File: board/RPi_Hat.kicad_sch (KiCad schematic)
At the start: 39 parts, among them J1 PiHat, SW1 Pushbutton, SW2 Pushbutton, SW3 Pushbutton, SW4 Pushbutton, SW5 Pushbutton, SW6 Pushbutton, SW7 Pushbutton, SW8 Pushbutton

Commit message: pcb_completly_wired
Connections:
- net Button 1: now also J1.36 (BCM16); no longer J1.22 (BCM25)
- net Button 2: now also J1.38 (BCM20_MOSI); no longer J1.24 (BCM8_CE0)
- net Button 3: now also J1.31 (BCM6); no longer J1.26 (BCM7_CE1)
- net Button 4: now also J1.35 (BCM19_MISO); no longer J1.28 (BCM1_ID_SC)
- net Button 6: now also J1.37 (BCM26); no longer J1.36 (BCM16)
- net Button 7: now also J1.33 (BCM13); no longer J1.38 (BCM20_MOSI)
- net Diode 3: now also J1.22 (BCM25); no longer J1.27 (BCM0_ID_SD)
- net Diode 4: now also J1.24 (BCM8_CE0); no longer J1.29 (BCM5)
- net Diode 5: now also J1.26 (BCM7_CE1); no longer J1.31 (BCM6)
- net Diode 6: now also J1.27 (BCM0_ID_SD); no longer J1.33 (BCM13)
- net Diode 7: now also J1.28 (BCM1_ID_SC); no longer J1.35 (BCM19_MISO)
- net Diode 8: now also J1.29 (BCM5); no longer J1.37 (BCM26)
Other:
- title: (none) -> Rasperry Pi Shield

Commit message: transistors
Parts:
- removed C1: 100n, HWP:C_0805, symbol HWP:C
- added Q1, Q2, Q3, Q4, Q5, Q6, Q7, Q8: (no value), symbol HWP:PMOS_GSD
- J1: value PiHat -> (none); footprint HWP:PiHeader -> (none)
- R10, R9: value 10k -> 4.7k
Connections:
- net +3V3: now also Q1.3 (D), Q2.3 (D), Q3.3 (D), Q4.3 (D), Q5.3 (D), Q6.3 (D), Q7.3 (D), Q8.3 (D)
- net Button 1: now also J1.33 (BCM13); no longer J1.36 (BCM16)
- net Button 2: now also J1.31 (BCM6); no longer J1.38 (BCM20_MOSI)
- net Button 3: now also J1.32 (BCM12); no longer J1.31 (BCM6)
- net Button 4: now also J1.29 (BCM5); no longer J1.35 (BCM19_MISO)
- net Button 5: now also J1.36 (BCM16); no longer J1.32 (BCM12)
- net Button 6: now also J1.35 (BCM19_MISO); no longer J1.37 (BCM26)
- net Button 7: now also J1.37 (BCM26); no longer J1.33 (BCM13)
- net Button 8: now also J1.38 (BCM20_MOSI); no longer J1.40 (BCM21_SCLK)
- net Diode 1: now also J1.15 (BCM22), Q1.1 (G); no longer J1.21 (BCM9_MISO), R11.1
- net Diode 2: now also J1.13 (BCM27_PCM_D), Q2.1 (G); no longer J1.23 (BCM11_SCLK), R12.1
- net Diode 3: now also J1.24 (BCM8_CE0), Q3.1 (G); no longer J1.22 (BCM25), R13.1
- net Diode 4: now also J1.23 (BCM11_SCLK), Q4.1 (G); no longer J1.24 (BCM8_CE0), R14.1
- net Diode 5: now also J1.22 (BCM25), Q5.1 (G); no longer J1.26 (BCM7_CE1), R15.1
- net Diode 6: now also J1.21 (BCM9_MISO), Q6.1 (G); no longer J1.27 (BCM0_ID_SD), R16.1
- net Diode 7: now also J1.27 (BCM0_ID_SD), Q7.1 (G); no longer J1.28 (BCM1_ID_SC), R17.1
- net Diode 8: now also J1.28 (BCM1_ID_SC), Q8.1 (G); no longer J1.29 (BCM5), R18.1
- new net: Q4.2 (S), R14.1
- new net: Q6.2 (S), R16.1
- new net: Q2.2 (S), R12.1
- new net: Q1.2 (S), R11.1
- new net: Q3.2 (S), R13.1
- new net: Q5.2 (S), R15.1
- new net: Q7.2 (S), R17.1
- new net: Q8.2 (S), R18.1
- no-connect marks 13 -> 11

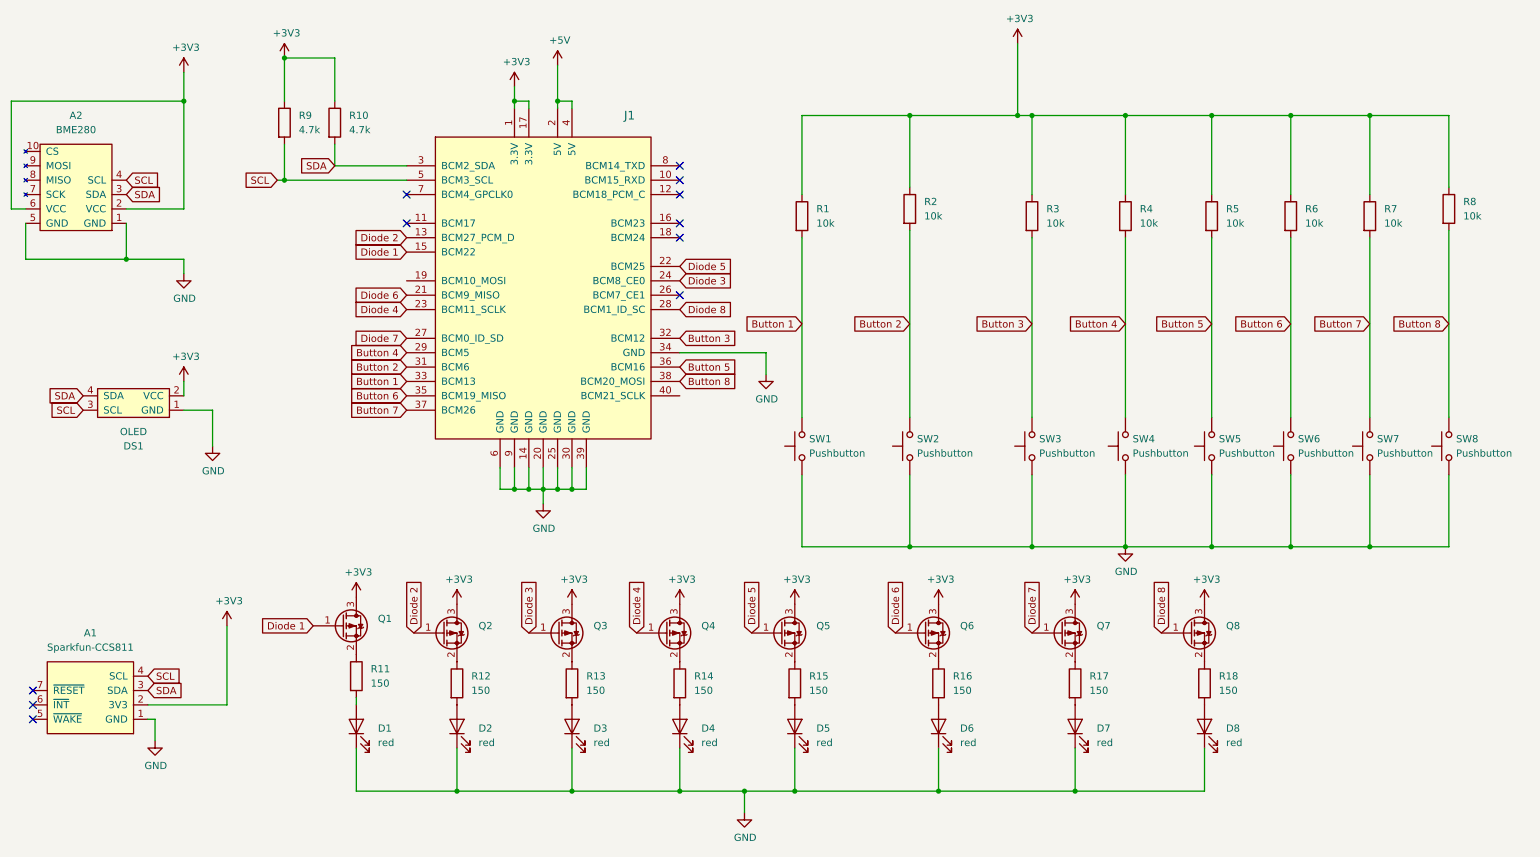
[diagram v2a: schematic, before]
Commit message: reinserted correct scematic
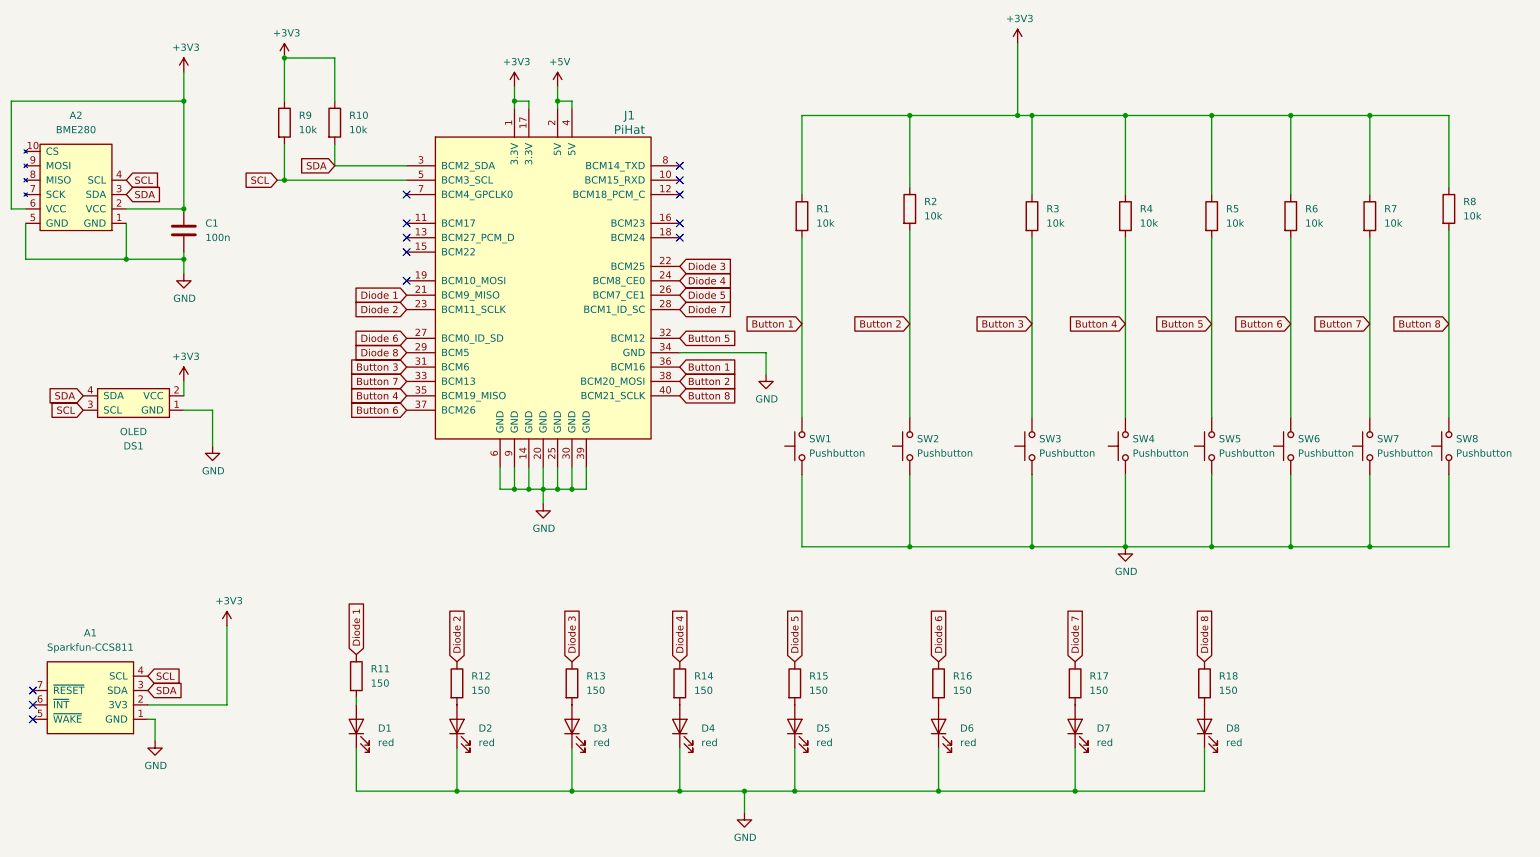
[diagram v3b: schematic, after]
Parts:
- removed Q1, Q2, Q3, Q4, Q5, Q6, Q7, Q8: (no value), symbol HWP:PMOS_GSD
- added C1: 100n, HWP:C_0805, symbol HWP:C
- J1: value (none) -> PiHat; footprint (none) -> HWP:PiHeader
- R10, R9: value 4.7k -> 10k
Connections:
- net +3V3: now also C1.1
- net Button 1: now also J1.36 (BCM16); no longer J1.33 (BCM13)
- net Button 2: now also J1.38 (BCM20_MOSI); no longer J1.31 (BCM6)
- net Button 3: now also J1.31 (BCM6); no longer J1.32 (BCM12)
- net Button 4: now also J1.35 (BCM19_MISO); no longer J1.29 (BCM5)
- net Button 5: now also J1.32 (BCM12); no longer J1.36 (BCM16)
- net Button 6: now also J1.37 (BCM26); no longer J1.35 (BCM19_MISO)
- net Button 7: now also J1.33 (BCM13); no longer J1.37 (BCM26)
- net Button 8: now also J1.40 (BCM21_SCLK); no longer J1.38 (BCM20_MOSI)
- net Diode 1: now also J1.21 (BCM9_MISO), R11.1; no longer J1.15 (BCM22)
- net Diode 2: now also J1.23 (BCM11_SCLK), R12.1; no longer J1.13 (BCM27_PCM_D)
- net Diode 3: now also J1.22 (BCM25), R13.1; no longer J1.24 (BCM8_CE0)
- net Diode 4: now also J1.24 (BCM8_CE0), R14.1; no longer J1.23 (BCM11_SCLK)
- net Diode 5: now also J1.26 (BCM7_CE1), R15.1; no longer J1.22 (BCM25)
- net Diode 6: now also J1.27 (BCM0_ID_SD), R16.1; no longer J1.21 (BCM9_MISO)
- net Diode 7: now also J1.28 (BCM1_ID_SC), R17.1; no longer J1.27 (BCM0_ID_SD)
- net Diode 8: now also J1.29 (BCM5), R18.1; no longer J1.28 (BCM1_ID_SC)
- net GND: now also C1.2
- no-connect marks 11 -> 13

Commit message: some bugfixing
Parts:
- removed C1: 100n, HWP:C_0805, symbol HWP:C
- R11, R12, R13, R14, R15, R16: value 150 -> (none); footprint HWP:R_0805 -> (none)
- R17: value 150 -> (none)
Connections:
- net Button 1: now also J1.33 (BCM13); no longer J1.36 (BCM16)
- net Button 2: now also J1.31 (BCM6); no longer J1.38 (BCM20_MOSI)
- net Button 3: now also J1.32 (BCM12); no longer J1.31 (BCM6)
- net Button 4: now also J1.29 (BCM5); no longer J1.35 (BCM19_MISO)
- net Button 5: now also J1.36 (BCM16); no longer J1.32 (BCM12)
- net Button 6: now also J1.35 (BCM19_MISO); no longer J1.37 (BCM26)
- net Button 7: now also J1.37 (BCM26); no longer J1.33 (BCM13)
- net Button 8: now also J1.38 (BCM20_MOSI); no longer J1.40 (BCM21_SCLK)
- net Diode 1: now also J1.13 (BCM27_PCM_D); no longer J1.21 (BCM9_MISO)
- net Diode 2: now also J1.11 (BCM17); no longer J1.23 (BCM11_SCLK)
- net Diode 3: now also J1.24 (BCM8_CE0); no longer J1.22 (BCM25)
- net Diode 4: now also J1.23 (BCM11_SCLK); no longer J1.24 (BCM8_CE0)
- net Diode 5: now also J1.15 (BCM22); no longer J1.26 (BCM7_CE1)
- net Diode 6: now also J1.19 (BCM10_MOSI); no longer J1.27 (BCM0_ID_SD)
- net Diode 7: now also J1.27 (BCM0_ID_SD); no longer J1.28 (BCM1_ID_SC)
- net Diode 8: now also J1.28 (BCM1_ID_SC); no longer J1.29 (BCM5)

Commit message: last minor changes
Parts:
- R18: value 150 -> (none); footprint HWP:R_0805 -> (none)
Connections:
- net Diode 3: now also J1.23 (BCM11_SCLK); no longer J1.24 (BCM8_CE0)
- net Diode 4: now also J1.21 (BCM9_MISO); no longer J1.23 (BCM11_SCLK)
- net Diode 7: now also J1.24 (BCM8_CE0); no longer J1.27 (BCM0_ID_SD)
- net Diode 8: now also J1.40 (BCM21_SCLK); no longer J1.28 (BCM1_ID_SC)
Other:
- company: t02 -> t02 Niko Fauter
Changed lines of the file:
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@@
     (title "Rasperry Pi Shield")
     (date "2022-05-11")
-    (company "t02")
+    (company "t02 Niko Fauter")
   )
   (junction (at 113.03 104.14) (diameter 0) (color 0 0 0 0)
@@
   (junction (at 115.57 35.56) (diameter 0) (color 0 0 0 0)
   )
-  (no_connect (at 88.9 69.85))
+  (no_connect (at 88.9 77.47))
   (no_connect (at 137.16 64.77))
-  (no_connect (at 137.16 69.85))
+  (no_connect (at 137.16 72.39))
   (no_connect (at 22.86 142.24))
   (no_connect (at 22.86 139.7))
   (no_connect (at 22.86 144.78))
-  (no_connect (at 137.16 87.63))
+  (no_connect (at 137.16 69.85))
   (no_connect (at 88.9 52.07))
   (no_connect (at 137.16 46.99))
@@
     )
   )
-  (global_label "Diode 7" (shape input) (at 88.9 77.47 180) (fields_autoplaced)
-    (effects (font (size 1.27 1.27)) (justify right))
-    (property "Intersheet References" "${INTERSHEET_REFS}" (id 0) (at 79.1372 77.3906 0)
-      (effects (font (size 1.27 1.27)) (justify right) hide)
+  (global_label "Diode 7" (shape input) (at 137.16 67.31 0) (fields_autoplaced)
+    (effects (font (size 1.27 1.27)) (justify left))
+    (property "Intersheet References" "${INTERSHEET_REFS}" (id 0) (at 146.9228 67.3894 0)
+      (effects (font (size 1.27 1.27)) (justify left) hide)
     )
   )
@@
     )
   )
-  (global_label "Diode 4" (shape input) (at 88.9 72.39 180) (fields_autoplaced)
-    (effects (font (size 1.27 1.27)) (justify right))
-    (property "Intersheet References" "${INTERSHEET_REFS}" (id 0) (at 79.1372 72.3106 0)
+  (global_label "Diode 4" (shape input) (at 88.9 69.85 180) (fields_autoplaced)
+    (effects (font (size 1.27 1.27)) (justify right))
+    (property "Intersheet References" "${INTERSHEET_REFS}" (id 0) (at 79.1372 69.7706 0)
       (effects (font (size 1.27 1.27)) (justify right) hide)
     )
@@
     )
   )
-  (global_label "Diode 3" (shape input) (at 137.16 67.31 0) (fields_autoplaced)
-    (effects (font (size 1.27 1.27)) (justify left))
-    (property "Intersheet References" "${INTERSHEET_REFS}" (id 0) (at 146.9228 67.3894 0)
-      (effects (font (size 1.27 1.27)) (justify left) hide)
+  (global_label "Diode 3" (shape input) (at 88.9 72.39 180) (fields_autoplaced)
+    (effects (font (size 1.27 1.27)) (justify right))
+    (property "Intersheet References" "${INTERSHEET_REFS}" (id 0) (at 79.1372 72.3106 0)
+      (effects (font (size 1.27 1.27)) (justify right) hide)
     )
   )
@@
     )
   )
-  (global_label "Diode 8" (shape input) (at 137.16 72.39 0) (fields_autoplaced)
+  (global_label "Diode 8" (shape input) (at 137.16 87.63 0) (fields_autoplaced)
     (effects (font (size 1.27 1.27)) (justify left))
-    (property "Intersheet References" "${INTERSHEET_REFS}" (id 0) (at 146.9228 72.3106 0)
+    (property "Intersheet References" "${INTERSHEET_REFS}" (id 0) (at 146.9228 87.5506 0)
       (effects (font (size 1.27 1.27)) (justify left) hide)
     )
@@
       (effects (font (size 1.27 1.27)) (justify left))
     )
-    (property "Value" "150" (id 1) (at 232.41 139.6999 0)
-      (effects (font (size 1.27 1.27)) (justify left))
-    )
-    (property "Footprint" "HWP:R_0805" (id 2) (at 228.092 138.43 90)
+    (property "Value" "" (id 1) (at 232.41 139.6999 0)
+      (effects (font (size 1.27 1.27)) (justify left))
+    )
+    (property "Footprint" "" (id 2) (at 228.092 138.43 90)
       (effects (font (size 1.27 1.27)) hide)
     )
@@
     )
     (path "/43ba65c3-454d-4594-82aa-ed537491184c"
-      (reference "R11") (unit 1) (value "200") (footprint "HWP:R_0805")
+      (reference "R11") (unit 1) (value "330") (footprint "HWP:R_0805")
     )
     (path "/318c77cd-628d-49c1-ae68-2df8f75dbca2"
-      (reference "R12") (unit 1) (value "200") (footprint "HWP:R_0805")
+      (reference "R12") (unit 1) (value "330") (footprint "HWP:R_0805")
     )
     (path "/9db069b6-7505-4811-820e-53465e7019e0"
-      (reference "R13") (unit 1) (value "200") (footprint "HWP:R_0805")
+      (reference "R13") (unit 1) (value "330") (footprint "HWP:R_0805")
     )
     (path "/1d0ab0e4-58a1-4d84-a3f9-9ce8cd8f9edc"
-      (reference "R14") (unit 1) (value "200") (footprint "HWP:R_0805")
+      (reference "R14") (unit 1) (value "330") (footprint "HWP:R_0805")
     )
     (path "/cc1e3c51-21f2-4224-9e28-f4519c566d85"
-      (reference "R15") (unit 1) (value "200") (footprint "HWP:R_0805")
+      (reference "R15") (unit 1) (value "330") (footprint "HWP:R_0805")
     )
     (path "/d85e13bc-11d3-4dd8-be68-895f4d019191"
-      (reference "R16") (unit 1) (value "200") (footprint "HWP:R_0805")
+      (reference "R16") (unit 1) (value "330") (footprint "HWP:R_0805")
     )
     (path "/b29c3a68-4ae8-4d50-993e-ad946a8406e0"
-      (reference "R17") (unit 1) (value "200") (footprint "HWP:R_0805")
+      (reference "R17") (unit 1) (value "330") (footprint "HWP:R_0805")
     )
     (path "/f516ae42-14f4-4c85-be33-6075d76673a9"
-      (reference "R18") (unit 1) (value "150") (footprint "HWP:R_0805")
+      (reference "R18") (unit 1) (value "330") (footprint "HWP:R_0805")
     )
     (path "/64fe4ef0-94d6-4168-93a5-da4cb1d6b68d"
